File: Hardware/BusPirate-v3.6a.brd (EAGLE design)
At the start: 60 x 37 mm, 47 parts, among them IC1 4066, J1 USB-MINIB-5PIN, U1 MIC5205 3V3, U2 MIC5205 3V3, U3 PIC24FJ64GA002, U4 MIC5205 5V0, U5 FT232RL-BASICSSOP

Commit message: Addressed issues
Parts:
- R1, R5, R8: value 0.27 -> 0
- renumbered IC1 to U6
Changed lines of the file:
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@@
 <setting verticaltext="up"/>
 </settings>
-<grid distance="0.05" unitdist="inch" unit="inch" style="lines" multiple="1" display="yes" altdistance="0.0005" altunitdist="inch" altunit="inch"/>
+<grid distance="0.1" unitdist="mil" unit="mil" style="lines" multiple="1" display="yes" altdistance="0.0005" altunitdist="inch" altunit="inch"/>
 <layers>
 <layer number="1" name="Top" color="4" fill="1" visible="yes" active="yes"/>
-<layer number="2" name="Route2" color="1" fill="3" visible="yes" active="yes"/>
-<layer number="3" name="Route3" color="4" fill="3" visible="yes" active="yes"/>
-<layer number="4" name="Route4" color="1" fill="4" visible="yes" active="yes"/>
-<layer number="5" name="Route5" color="4" fill="4" visible="yes" active="yes"/>
-<layer number="6" name="Route6" color="1" fill="8" visible="yes" active="yes"/>
-<layer number="7" name="Route7" color="4" fill="8" visible="yes" active="yes"/>
-<layer number="8" name="Route8" color="1" fill="2" visible="yes" active="yes"/>
-<layer number="9" name="Route9" color="4" fill="2" visible="yes" active="yes"/>
-<layer number="10" name="Route10" color="1" fill="7" visible="yes" active="yes"/>
-<layer number="11" name="Route11" color="4" fill="7" visible="yes" active="yes"/>
-<layer number="12" name="Route12" color="1" fill="5" visible="yes" active="yes"/>
-<layer number="13" name="Route13" color="4" fill="5" visible="yes" active="yes"/>
-<layer number="14" name="Route14" color="1" fill="6" visible="yes" active="yes"/>
-<layer number="15" name="Route15" color="4" fill="6" visible="yes" active="yes"/>
+<layer number="2" name="Route2" color="1" fill="3" visible="no" active="yes"/>
+<layer number="3" name="Route3" color="4" fill="3" visible="no" active="yes"/>
+<layer number="4" name="Route4" color="1" fill="4" visible="no" active="yes"/>
+<layer number="5" name="Route5" color="4" fill="4" visible="no" active="yes"/>
+<layer number="6" name="Route6" color="1" fill="8" visible="no" active="yes"/>
+<layer number="7" name="Route7" color="4" fill="8" visible="no" active="yes"/>
+<layer number="8" name="Route8" color="1" fill="2" visible="no" active="yes"/>
+<layer number="9" name="Route9" color="4" fill="2" visible="no" active="yes"/>
+<layer number="10" name="Route10" color="1" fill="7" visible="no" active="yes"/>
+<layer number="11" name="Route11" color="4" fill="7" visible="no" active="yes"/>
+<layer number="12" name="Route12" color="1" fill="5" visible="no" active="yes"/>
+<layer number="13" name="Route13" color="4" fill="5" visible="no" active="yes"/>
+<layer number="14" name="Route14" color="1" fill="6" visible="no" active="yes"/>
+<layer number="15" name="Route15" color="4" fill="6" visible="no" active="yes"/>
 <layer number="16" name="Bottom" color="1" fill="1" visible="yes" active="yes"/>
 <layer number="17" name="Pads" color="2" fill="1" visible="yes" active="yes"/>
@@
 <layer number="27" name="tValues" color="7" fill="1" visible="no" active="yes"/>
 <layer number="28" name="bValues" color="7" fill="1" visible="no" active="yes"/>
-<layer number="29" name="tStop" color="7" fill="3" visible="no" active="yes"/>
-<layer number="30" name="bStop" color="7" fill="6" visible="no" active="yes"/>
+<layer number="29" name="tStop" color="7" fill="3" visible="yes" active="yes"/>
+<layer number="30" name="bStop" color="7" fill="6" visible="yes" active="yes"/>
 <layer number="31" name="tCream" color="7" fill="4" visible="no" active="yes"/>
 <layer number="32" name="bCream" color="7" fill="5" visible="no" active="yes"/>
@@
 <text x="29.845" y="-8.89" size="1.778" layer="51" font="vector" align="bottom-center">Released under the Creative Commons 0 "No Rights Reserved"</text>
 <text x="29.845" y="-11.43" size="1.778" layer="51" font="vector" align="bottom-center">https://creativecommons.org/publicdomain/zero/1.0/</text>
+<circle x="14.828521875" y="29.4386" radius="0.532025" width="0" layer="30"/>
 </plain>
 <attributes>
@@
 <attribute name="PROD_ID" value="NDUC-12579" x="12.7" y="27.4955" size="1.778" layer="27" rot="R90" display="off"/>
 </element>
-<element name="IC1" library="40xx" package="TSSOP14" value="4066" x="43.657" y="5.63" smashed="yes" rot="R270">
+<element name="U6" library="40xx" package="TSSOP14" value="4066" x="43.657" y="5.63" smashed="yes" rot="R270">
 <attribute name="NAME" x="43.5808" y="8.3986" size="1.016" layer="25" font="vector" ratio="12"/>
 <attribute name="VALUE" x="43.022" y="9.186" size="1.27" layer="27" font="vector" ratio="10" rot="R270"/>
@@
 <attribute name="PROD_ID" value="CONN-09508" x="51.5" y="18.5" size="1.778" layer="27" display="off"/>
 </element>
-<element name="R1" library="SparkFun-Resistors" package="0603" value="0.27" x="2.9464" y="26.924" rot="R270">
+<element name="R1" library="SparkFun-Resistors" package="0603" value="0" x="2.9464" y="26.924" rot="R270">
 <attribute name="PROD_ID" value="RES-08787" x="2.9464" y="26.924" size="1.778" layer="27" rot="R270" display="off"/>
 </element>
-<element name="R5" library="SparkFun-Resistors" package="0603" value="0.27" x="34.544" y="27.0256" rot="R270">
+<element name="R5" library="SparkFun-Resistors" package="0603" value="0" x="34.544" y="27.0256" rot="R270">
 <attribute name="PROD_ID" value="RES-08787" x="34.544" y="27.0256" size="1.778" layer="27" rot="R270" display="off"/>
 </element>
-<element name="R8" library="SparkFun-Resistors" package="0603" value="0.27" x="26.3652" y="27.1526" rot="R270">
+<element name="R8" library="SparkFun-Resistors" package="0603" value="0" x="26.3652" y="27.1526" rot="R270">
 <attribute name="PROD_ID" value="RES-08787" x="26.3652" y="27.1526" size="1.778" layer="27" rot="R270" display="off"/>
 </element>
@@
 <contactref element="LED7" pad="C"/>
 <contactref element="C5" pad="2"/>
-<contactref element="IC1" pad="7"/>
+<contactref element="U6" pad="7"/>
 <contactref element="C6" pad="2"/>
 <contactref element="LED6" pad="C"/>
@@
 </signal>
 <signal name="VEXTERN">
-<contactref element="IC1" pad="11"/>
-<contactref element="IC1" pad="8"/>
-<contactref element="IC1" pad="4"/>
-<contactref element="IC1" pad="1"/>
+<contactref element="U6" pad="11"/>
+<contactref element="U6" pad="8"/>
+<contactref element="U6" pad="4"/>
+<contactref element="U6" pad="1"/>
 <contactref element="R3" pad="8"/>
 <wire x1="45.607" y1="3.68" x2="46.582" y2="3.68" width="0.3048" layer="1"/>
@@
 </signal>
 <signal name="PULLUPEN">
-<contactref element="IC1" pad="5"/>
-<contactref element="IC1" pad="6"/>
-<contactref element="IC1" pad="12"/>
+<contactref element="U6" pad="5"/>
+<contactref element="U6" pad="6"/>
+<contactref element="U6" pad="12"/>
 <contactref element="R12" pad="4"/>
 <contactref element="U3" pad="22"/>
-<contactref element="IC1" pad="13"/>
+<contactref element="U6" pad="13"/>
 <wire x1="42.555" y1="5.544" x2="42.555" y2="6.265" width="0.3048" layer="1"/>
 <wire x1="42.006" y1="4.995" x2="42.555" y2="5.544" width="0.3048" layer="1"/>
@@
 <contactref element="C5" pad="1"/>
 <contactref element="L1" pad="2"/>
-<contactref element="IC1" pad="14"/>
+<contactref element="U6" pad="14"/>
 <contactref element="C6" pad="1"/>
 <contactref element="R12" pad="5"/>
@@
 </signal>
 <signal name="N$1">
-<contactref element="IC1" pad="2"/>
+<contactref element="U6" pad="2"/>
 <contactref element="R11" pad="2"/>
 <wire x1="38.9326" y1="14.647" x2="40.267" y2="14.647" width="0.3048" layer="1"/>
@@
 </signal>
 <signal name="N$5">
-<contactref element="IC1" pad="3"/>
+<contactref element="U6" pad="3"/>
 <contactref element="R12" pad="8"/>
 <wire x1="39.197" y1="6.28" x2="40.732" y2="6.28" width="0.3048" layer="1"/>
@@
 </signal>
 <signal name="N$2">
-<contactref element="IC1" pad="9"/>
+<contactref element="U6" pad="9"/>
 <contactref element="R12" pad="6"/>
 <wire x1="46.582" y1="4.33" x2="49.275" y2="4.33" width="0.3048" layer="1"/>
@@
 </signal>
 <signal name="N$4">
-<contactref element="IC1" pad="10"/>
+<contactref element="U6" pad="10"/>
 <contactref element="R12" pad="7"/>
 <wire x1="46.582" y1="4.98" x2="47.833" y2="4.98" width="0.3048" layer="1"/>

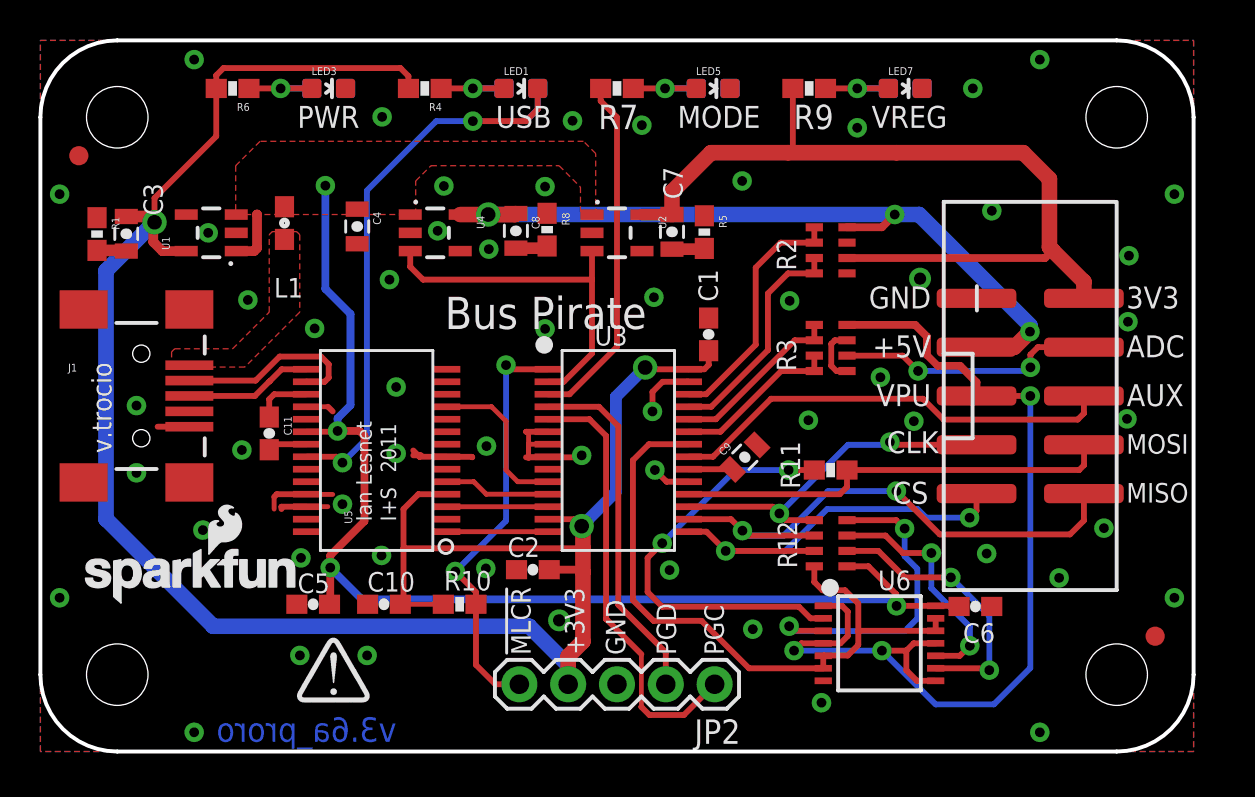
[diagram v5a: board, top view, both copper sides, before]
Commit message: Imported DP PCB part, and changed DRC to allow mask to cover large vias.
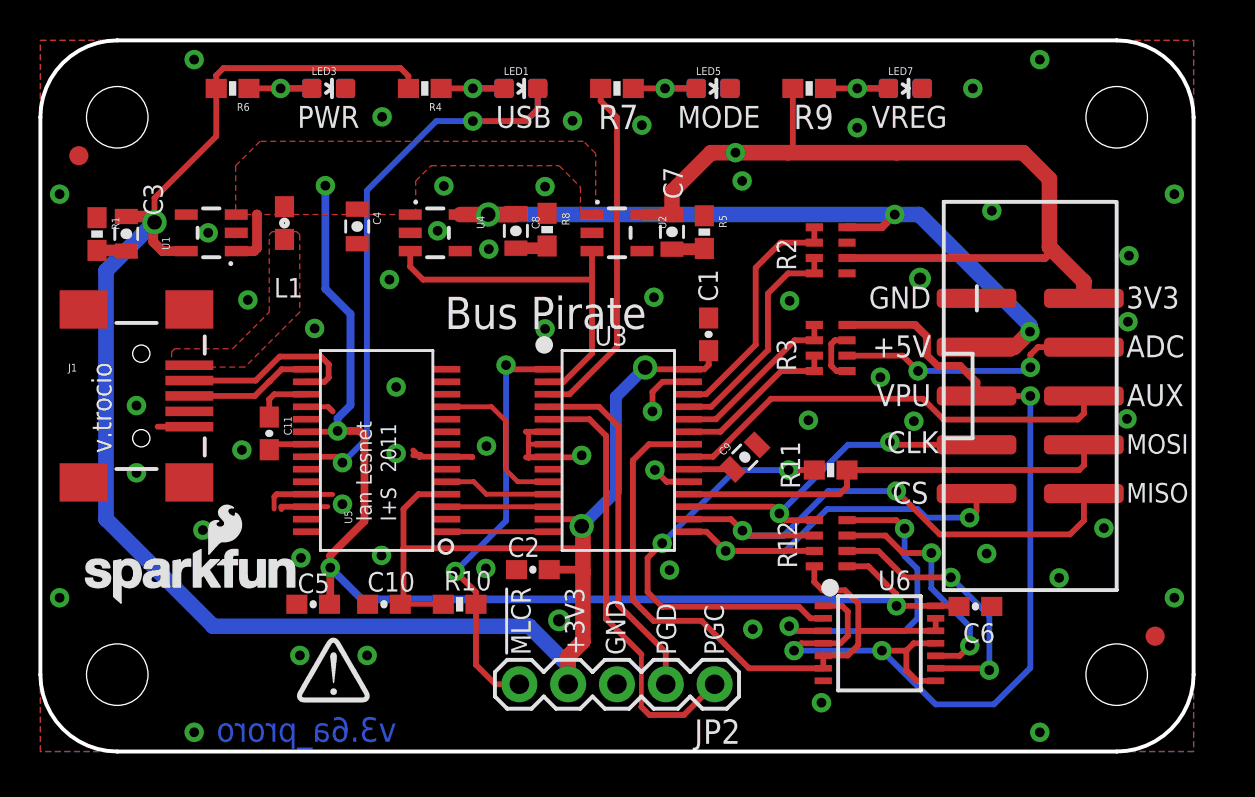
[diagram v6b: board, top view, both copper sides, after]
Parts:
- added PCB1: PCB_DP_RECTANGLE-37X60, SparkFun-Boards:DP6037_V1
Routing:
- net SW3V3: vias 0 -> 1
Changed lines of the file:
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@@
 <setting verticaltext="up"/>
 </settings>
-<grid distance="0.1" unitdist="mil" unit="mil" style="lines" multiple="1" display="yes" altdistance="0.0005" altunitdist="inch" altunit="inch"/>
+<grid distance="5" unitdist="mil" unit="mil" style="lines" multiple="1" display="yes" altdistance="0.0005" altunitdist="inch" altunit="inch"/>
 <layers>
 <layer number="1" name="Top" color="4" fill="1" visible="yes" active="yes"/>
@@
 <layer number="113" name="IDFDebug" color="4" fill="1" visible="no" active="yes"/>
 <layer number="114" name="Badge_Outline" color="11" fill="1" visible="no" active="no"/>
+<layer number="115" name="ReferenceISLANDS" color="7" fill="1" visible="yes" active="yes"/>
 <layer number="116" name="Patch_BOT" color="7" fill="1" visible="no" active="yes"/>
 <layer number="118" name="Rect_Pads" color="7" fill="1" visible="no" active="yes"/>
@@
 <vertex x="23.9" y="5.8175"/>
 </polygon>
-<wire x1="4" y1="37" x2="56" y2="37" width="0.2032" layer="20"/>
-<wire x1="56" y1="37" x2="60" y2="33" width="0.2032" layer="20" curve="-90"/>
-<wire x1="60" y1="33" x2="60" y2="4" width="0.2032" layer="20"/>
-<wire x1="60" y1="4" x2="56" y2="0" width="0.2032" layer="20" curve="-90"/>
-<wire x1="56" y1="0" x2="4" y2="0" width="0.2032" layer="20"/>
-<wire x1="4" y1="0" x2="0" y2="4" width="0.2032" layer="20" curve="-90"/>
-<wire x1="0" y1="4" x2="0" y2="33" width="0.2032" layer="20"/>
-<wire x1="0" y1="33" x2="4" y2="37" width="0.2032" layer="20" curve="-90"/>
-<wire x1="0" y1="4" x2="4" y2="0" width="0" layer="20" curve="90"/>
-<wire x1="56" y1="0" x2="60" y2="4" width="0" layer="20" curve="90"/>
-<wire x1="4" y1="37" x2="0" y2="33" width="0" layer="20" curve="90"/>
-<wire x1="56" y1="37" x2="60" y2="33" width="0" layer="20" curve="-90"/>
 <wire x1="54.75" y1="19.5" x2="54.75" y2="17.5" width="0" layer="49"/>
 <wire x1="5.25" y1="19.5" x2="5.25" y2="17.5" width="0" layer="49"/>
@@
 <wire x1="4" y1="0.85" x2="0.85" y2="4" width="1.7" layer="39" curve="-90"/>
 <wire x1="4" y1="0.85" x2="0.85" y2="4" width="1.7" layer="40" curve="-90"/>
-<hole x="4" y="4" drill="3.2"/>
-<hole x="56" y="4" drill="3.2"/>
-<hole x="56" y="33" drill="3.2"/>
-<hole x="4" y="33" drill="3.2"/>
 <polygon width="0" layer="41">
 <vertex x="7" y="37"/>
@@
 <text x="29.845" y="-8.89" size="1.778" layer="51" font="vector" align="bottom-center">Released under the Creative Commons 0 "No Rights Reserved"</text>
 <text x="29.845" y="-11.43" size="1.778" layer="51" font="vector" align="bottom-center">https://creativecommons.org/publicdomain/zero/1.0/</text>
-<circle x="14.828521875" y="29.4386" radius="0.532025" width="0" layer="30"/>
+<circle x="14.828521875" y="29.4386" radius="0.6096" width="0" layer="30"/>
+<circle x="23.2982" y="27.94" radius="0.7366" width="0" layer="30"/>
+<circle x="5.938" y="27.5375" radius="0.7366" width="0" layer="30"/>
+<circle x="36.164521875" y="31.1531" radius="0.6096" width="0" layer="30"/>
 </plain>
 <attributes>
@@
 </class>
 </classes>
-<designrules name="SparkFun-2-layer">
+<designrules name="SparkFun-2-layer *">
 <description language="en">&lt;b&gt;EAGLE Design Rules&lt;/b&gt;
 &lt;p&gt;
@@
 <param name="mlMinCreamFrame" value="0mil"/>
 <param name="mlMaxCreamFrame" value="0mil"/>
-<param name="mlViaStopLimit" value="20mil"/>
+<param name="mlViaStopLimit" value="30mil"/>
 <param name="srRoundness" value="0"/>
 <param name="srMinRoundness" value="0mil"/>
@@
 <attribute name="PROD_ID" value="CAP-11330" x="16.4846" y="27.3177" size="1.778" layer="27" rot="R270" display="off"/>
 </element>
+<element name="PCB1" library="SparkFun-Boards" package="DP6037_V1" value="PCB_DP_RECTANGLE-37X60" x="0" y="0"/>
 </elements>
 <signals>
@@
 <contactref element="R2" pad="6"/>
 <contactref element="U2" pad="5"/>
-<wire x1="34.894" y1="31.157" x2="38.9" y2="31.157" width="0.8128" layer="1"/>
+<wire x1="34.894" y1="31.157" x2="36.164" y2="31.157" width="0.8128" layer="1"/>
+<wire x1="36.164" y1="31.157" x2="38.9" y2="31.157" width="0.8128" layer="1"/>
 <wire x1="38.9" y1="31.157" x2="44.546" y2="31.157" width="0.8128" layer="1"/>
 <wire x1="32.862" y1="27.9383" x2="32.862" y2="29.125" width="0.8128" layer="1"/>
@@
 <wire x1="31.3001" y1="27.9375" x2="32.862" y2="27.9375" width="0.6096" layer="1"/>
 <wire x1="32.862" y1="27.9375" x2="32.862" y2="27.9383" width="0.6096" layer="1"/>
+<via x="36.164" y="31.157" extent="1-16" drill="0.508"/>
 </signal>
 <signal name="SW5V0">

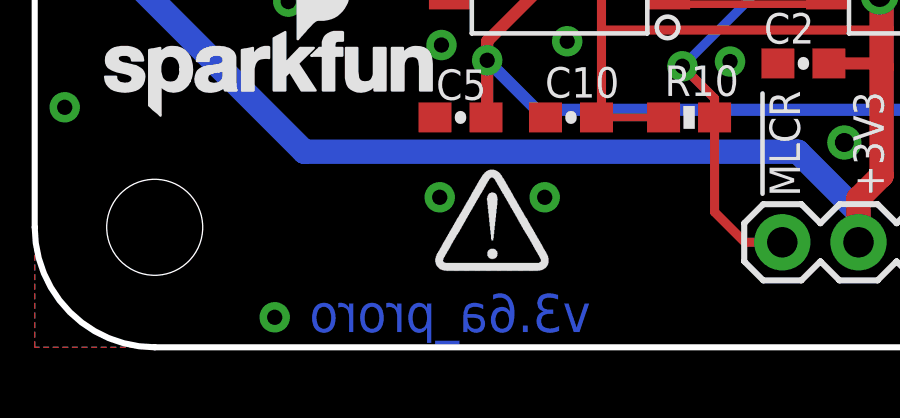
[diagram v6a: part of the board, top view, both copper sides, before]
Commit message: Changed one PROD_ID and version number
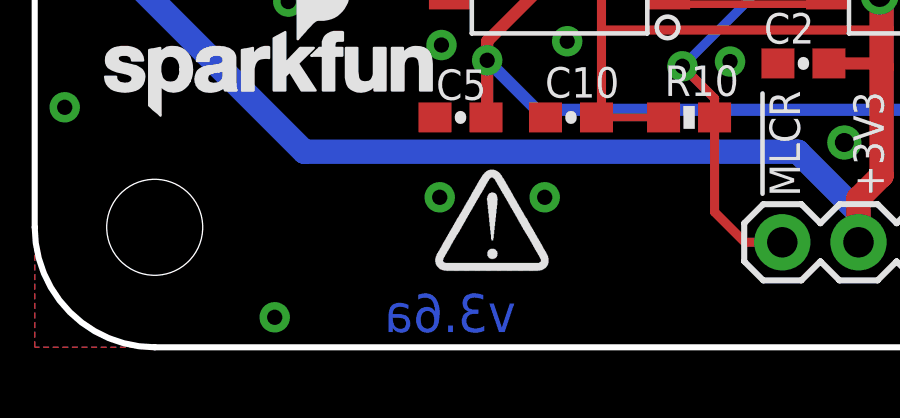
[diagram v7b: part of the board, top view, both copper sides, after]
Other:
- board text added: "v3.6a"
- board text removed: "v3.6a_proro"
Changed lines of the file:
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@@
 <text x="29.845" y="-13.97" size="1.778" layer="51" font="vector" align="bottom-center">Designed by: Ian Lesnet http://dangerousprototypes.com</text>
 <text x="29.845" y="-16.54175" size="1.778" layer="51" font="vector" align="bottom-center">Revised by: Brent Wilkins (Based on BP v3.6a)</text>
-<text x="13.843" y="0.508" size="1.27" layer="16" font="vector" ratio="18" rot="MR0" align="bottom-center">v3.6a_proro</text>
+<text x="13.843" y="0.508" size="1.27" layer="16" font="vector" ratio="18" rot="MR0" align="bottom-center">v3.6a</text>
 <text x="14.986" y="33.02" size="1.143" layer="21" font="vector" ratio="15" align="center">PWR</text>
 <text x="25.146" y="33.02" size="1.143" layer="21" font="vector" ratio="15" align="center">USB</text>
@@
 <attribute name="NAME" x="43.5808" y="8.3986" size="1.016" layer="25" font="vector" ratio="12"/>
 <attribute name="VALUE" x="43.022" y="9.186" size="1.27" layer="27" font="vector" ratio="10" rot="R270"/>
-<attribute name="PROD_ID" value="IC-09427" x="43.657" y="5.63" size="1.778" layer="27" rot="R270" display="off"/>
+<attribute name="PROD_ID" value="IC-13191" x="43.657" y="5.63" size="1.778" layer="27" rot="R270" display="off"/>
 </element>
 <element name="C6" library="SparkFun-Capacitors" package="0603-CAP" value="0.1uF" x="48.6481" y="7.5477" smashed="yes">

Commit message: Corrected resistor value
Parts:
- R1, R5, R8: value 0 -> 0.27
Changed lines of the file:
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@@
 <attribute name="PROD_ID" value="CONN-09508" x="51.5" y="18.5" size="1.778" layer="27" display="off"/>
 </element>
-<element name="R1" library="SparkFun-Resistors" package="0603" value="0" x="2.9464" y="26.924" rot="R270">
+<element name="R1" library="SparkFun-Resistors" package="0603" value="0.27" x="2.9464" y="26.924" rot="R270">
 <attribute name="PROD_ID" value="RES-08787" x="2.9464" y="26.924" size="1.778" layer="27" rot="R270" display="off"/>
 </element>
-<element name="R5" library="SparkFun-Resistors" package="0603" value="0" x="34.544" y="27.0256" rot="R270">
+<element name="R5" library="SparkFun-Resistors" package="0603" value="0.27" x="34.544" y="27.0256" rot="R270">
 <attribute name="PROD_ID" value="RES-08787" x="34.544" y="27.0256" size="1.778" layer="27" rot="R270" display="off"/>
 </element>
-<element name="R8" library="SparkFun-Resistors" package="0603" value="0" x="26.3652" y="27.1526" rot="R270">
+<element name="R8" library="SparkFun-Resistors" package="0603" value="0.27" x="26.3652" y="27.1526" rot="R270">
 <attribute name="PROD_ID" value="RES-08787" x="26.3652" y="27.1526" size="1.778" layer="27" rot="R270" display="off"/>
 </element>
